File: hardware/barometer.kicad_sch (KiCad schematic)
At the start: 3 parts, among them U4 BMP581

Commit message: feat(kicad): Cleared ERC errors and assigned footprints for all parts
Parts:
- C20, C21: footprint Capacitor_SMD:C_0603_1608Metric -> Capacitor_SMD:C_0402_1005Metric
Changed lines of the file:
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@@
 			)
 		)
-		(property "Footprint" "Capacitor_SMD:C_0603_1608Metric"
+		(property "Footprint" "Capacitor_SMD:C_0402_1005Metric"
 			(at 181.3052 92.71 0)
 			(hide yes)
@@
 			)
 		)
-		(property "Footprint" "Capacitor_SMD:C_0603_1608Metric"
+		(property "Footprint" "Capacitor_SMD:C_0402_1005Metric"
 			(at 107.6452 93.98 0)
 			(hide yes)

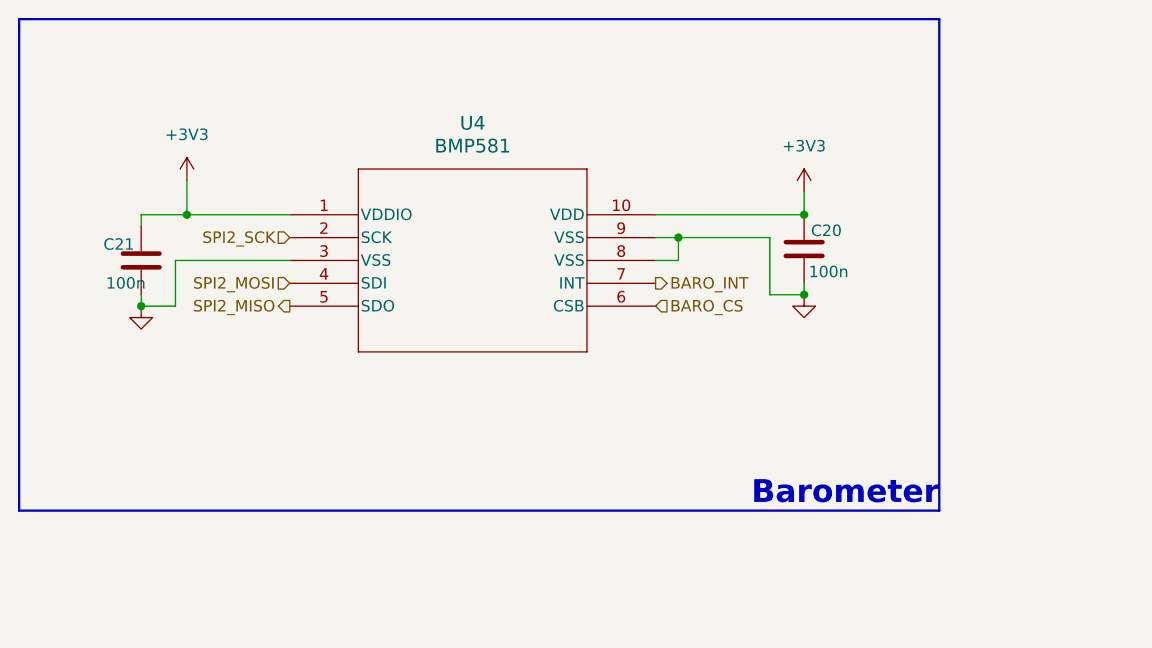
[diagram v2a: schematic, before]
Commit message: feat(kicad): Added Barometer application notes
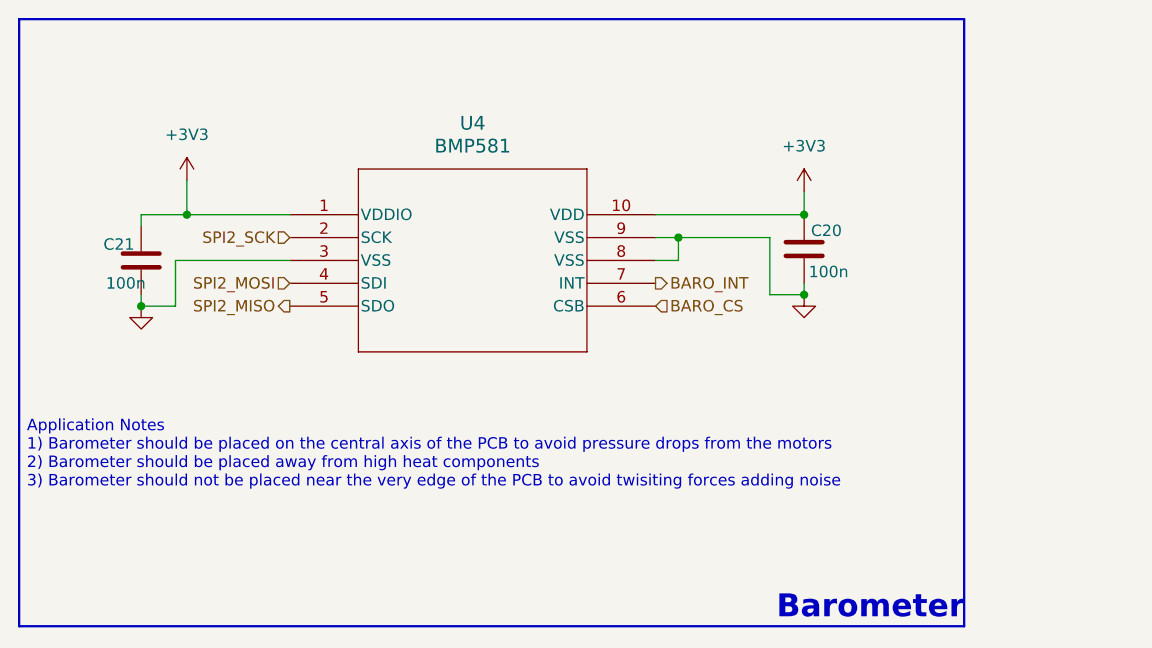
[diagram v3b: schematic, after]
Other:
- note added: "Application Notes 1) Barometer should be placed on the central axis of the PCB to avoid pressure drops from the motors 2) Barometer should be placed away from high heat components 3) Barometer should not be placed near the very edge of the PCB to avoid twisiting forces adding noise"
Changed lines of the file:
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@@
 	(rectangle
 		(start 93.1188 63.357)
-		(end 195.3538 117.967)
+		(end 198.12 130.81)
 		(stroke
 			(width 0.254)
@@
 		)
 	)
+	(text "Application Notes\n1) Barometer should be placed on the central axis of the PCB to avoid pressure drops from the motors\n2) Barometer should be placed away from high heat components\n3) Barometer should not be placed near the very edge of the PCB to avoid twisiting forces adding noise"
+		(exclude_from_sim no)
+		(at 93.98 111.76 0)
+		(effects
+			(font
+				(size 1.27 1.27)
+			)
+			(justify left)
+		)
+	)
 	(text "Barometer\n"
 		(exclude_from_sim no)
-		(at 184.912 116.078 0)
+		(at 187.706 128.778 0)
 		(effects
 			(font

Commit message: feat(kicad): Updated schematic to keep traces shorter on the layout Restarting layout
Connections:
- net SPI2_MISO renamed SPI3_MISO
- net SPI2_MOSI renamed SPI3_MOSI
- net SPI2_SCK renamed SPI3_SCK
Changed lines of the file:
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@@
 		)
 	)
-	(hierarchical_label "SPI2_MOSI"
+	(hierarchical_label "SPI3_MOSI"
 		(shape input)
 		(at 123.19 92.71 180)
@@
 		)
 	)
-	(hierarchical_label "SPI2_MISO"
+	(hierarchical_label "SPI3_MISO"
 		(shape output)
 		(at 123.19 95.25 180)
@@
 		)
 	)
-	(hierarchical_label "SPI2_SCK"
+	(hierarchical_label "SPI3_SCK"
 		(shape input)
 		(at 123.19 87.63 180)

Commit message: feat(kicad): Routing complete, assigning jlc components to each footprint
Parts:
- C20, C21: LCSC (none) -> C1525
- U4: LCSC (none) -> C5362283
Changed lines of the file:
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@@
+			)
+		)
+		(property "LCSC" "C1525"
+			(at 180.34 88.9 0)
+			(hide yes)
+			(show_name no)
+			(do_not_autoplace no)
+			(effects
+				(font
+					(size 1.27 1.27)
+				)
+			)
+		)
+		(property "KLC_S3.3" ""
+			(at 180.34 88.9 0)
+			(hide yes)
+			(show_name no)
+			(do_not_autoplace no)
+			(effects
+				(font
+					(size 1.27 1.27)
+				)
+			)
+		)
+		(property "KLC_S4.1" ""
+			(at 180.34 88.9 0)
+			(hide yes)
+			(show_name no)
+			(do_not_autoplace no)
+			(effects
+				(font
+					(size 1.27 1.27)
+				)
 			)
 		)
@@
 			)
 		)
+		(property "LCSC" "C1525"
+			(at 106.68 90.17 0)
+			(hide yes)
+			(show_name no)
+			(do_not_autoplace no)
+			(effects
+				(font
+					(size 1.27 1.27)
+				)
+			)
+		)
+		(property "KLC_S3.3" ""
+			(at 106.68 90.17 0)
+			(hide yes)
+			(show_name no)
+			(do_not_autoplace no)
+			(effects
+				(font
+					(size 1.27 1.27)
+				)
+			)
+		)
+		(property "KLC_S4.1" ""
+			(at 106.68 90.17 0)
+			(hide yes)
+			(show_name no)
+			(do_not_autoplace no)
+			(effects
+				(font
+					(size 1.27 1.27)
+				)
+			)
+		)
 		(pin "1"
 		)
@@
 			(at 123.19 85.09 0)
 			(hide yes)
+			(show_name no)
+			(do_not_autoplace no)
+			(effects
+				(font
+					(size 1.27 1.27)
+				)
+			)
+		)
+		(property "LCSC" "C5362283"
+			(at 123.19 85.09 0)
+			(hide yes)
+			(show_name no)
+			(do_not_autoplace no)
+			(effects
+				(font
+					(size 1.27 1.27)
+				)
+			)
+		)
+		(property "KLC_S3.3" ""
+			(at 123.19 85.09 0)
+			(hide yes)
+			(show_name no)
+			(do_not_autoplace no)
+			(effects
+				(font
+					(size 1.27 1.27)
+				)
+			)
+		)
+		(property "KLC_S4.1" ""
+			(at 123.19 85.09 0)
+			(hide yes)
